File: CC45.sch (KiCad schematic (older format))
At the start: 20 parts

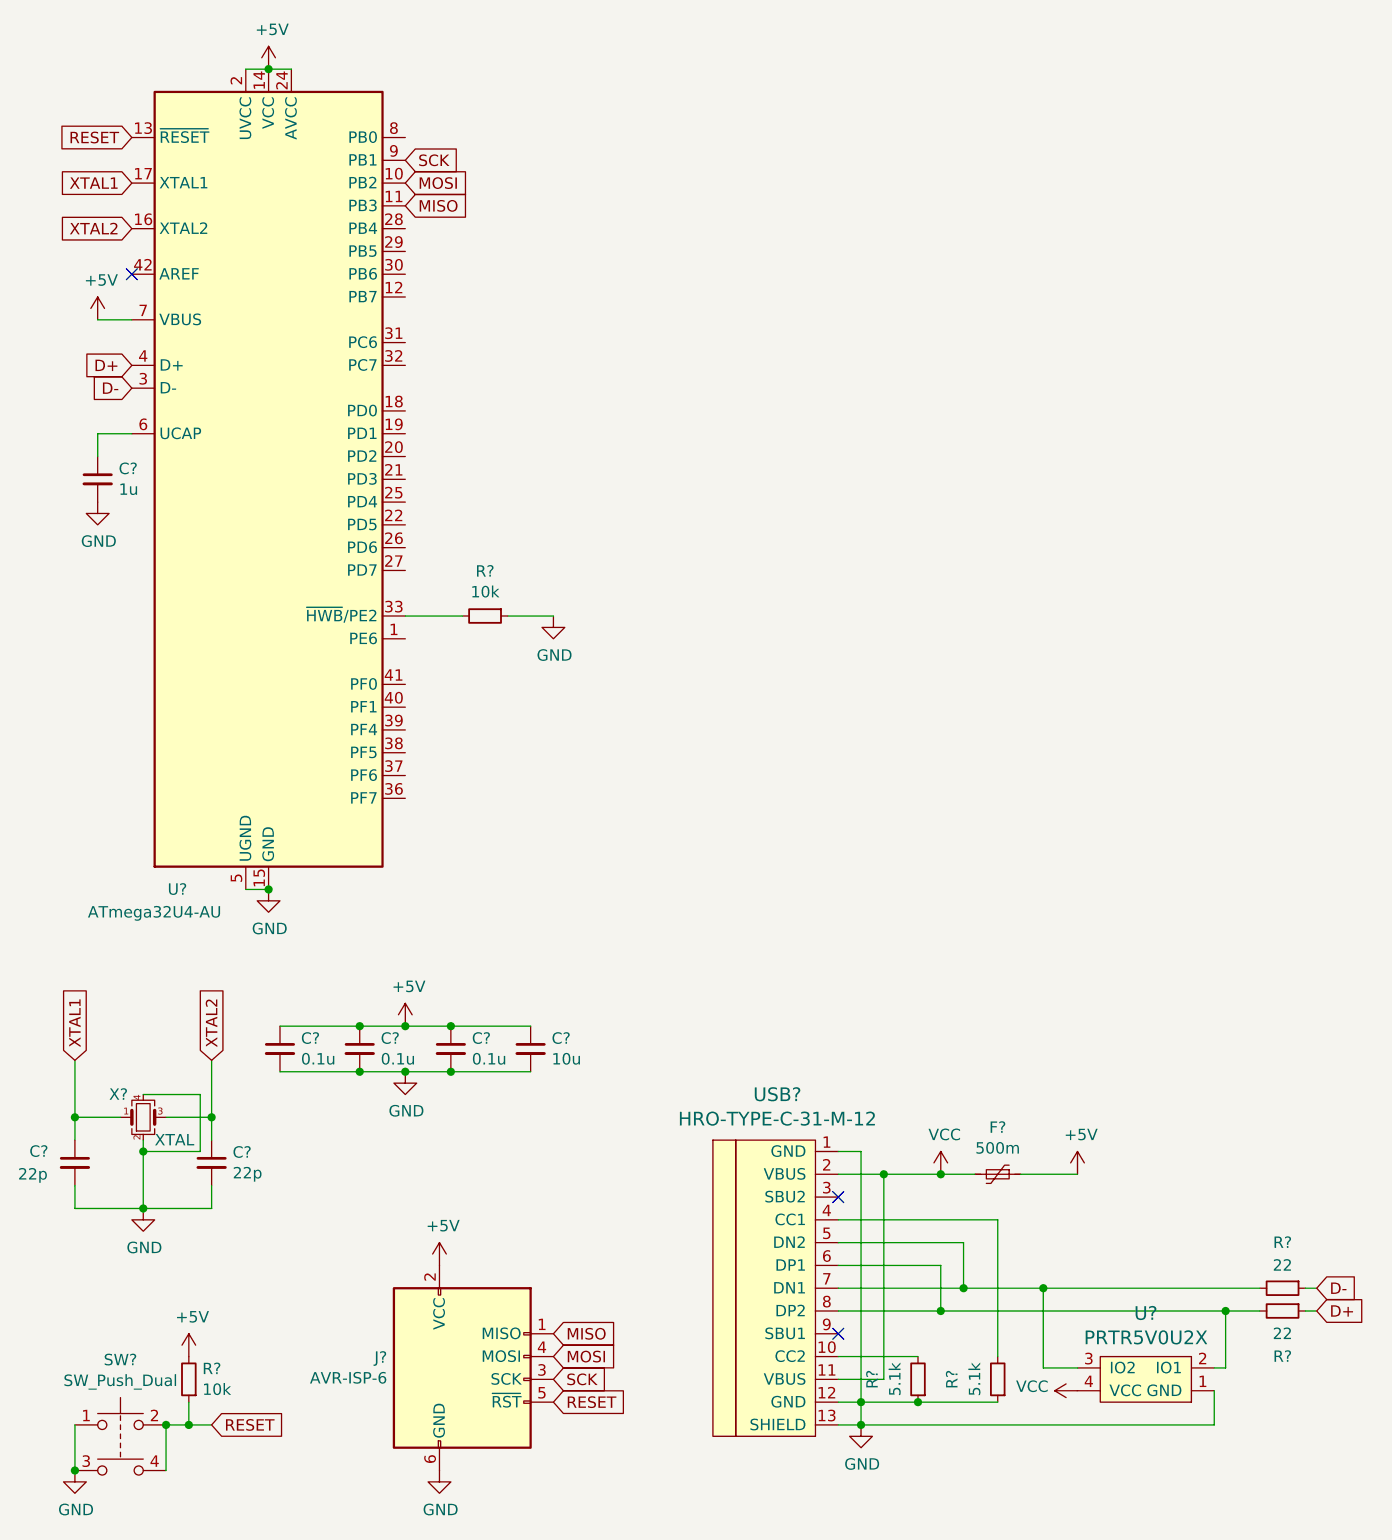
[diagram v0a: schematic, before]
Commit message: add switch matrix and assign footprints
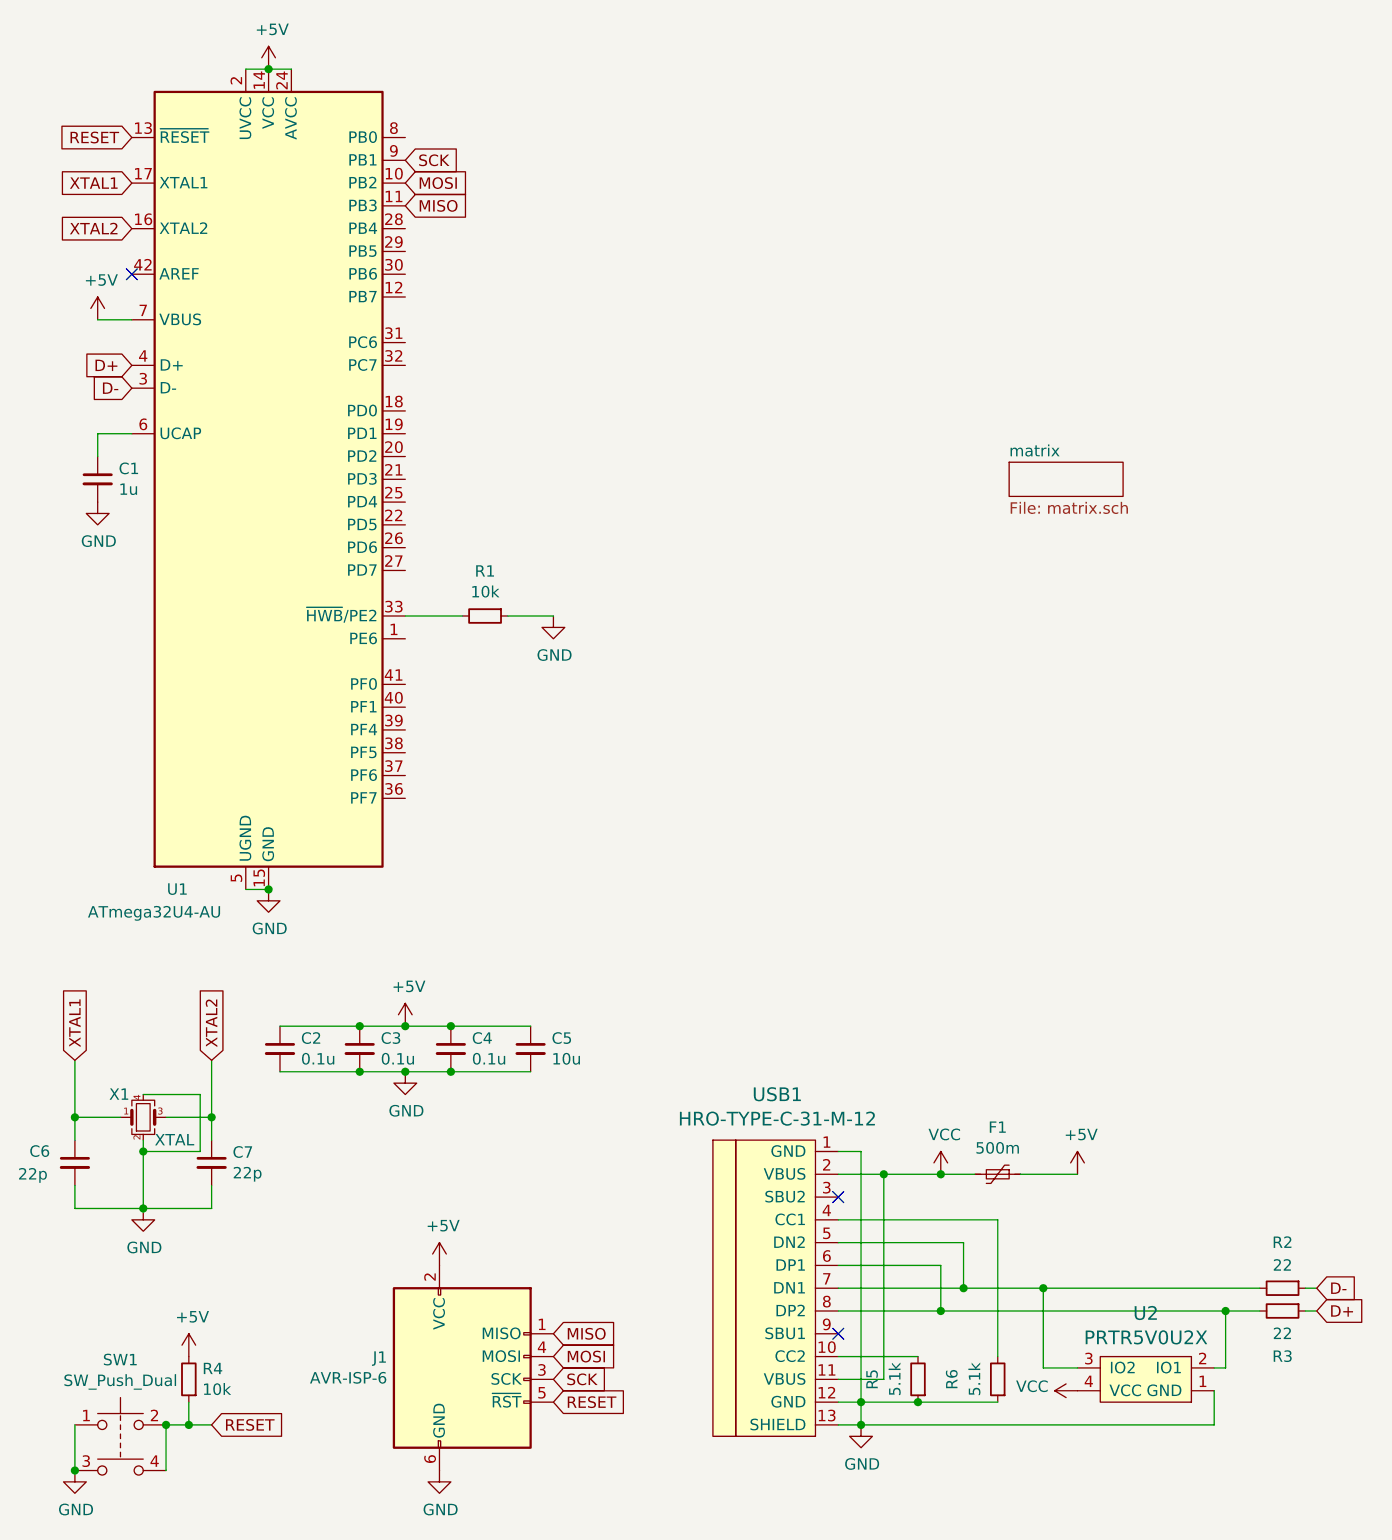
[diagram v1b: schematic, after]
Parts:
- removed C? (x2): 22p, symbol Device:C_Small
- removed C? (x2): 0.1u, symbol Device:C_Small
- removed R? (x2): 5.1k, symbol Device:R_Small
- removed R? (x2): 22, symbol Device:R_Small
- added C2, C3: 0.1u, Capacitor_SMD:C_1206_3216Metric_Pad1.42x1.75mm_HandSolder, symbol Device:C_Small
- added C6, C7: 22p, Capacitor_SMD:C_1206_3216Metric_Pad1.42x1.75mm_HandSolder, symbol Device:C_Small
- added R2, R3: 22, Resistor_SMD:R_1206_3216Metric_Pad1.42x1.75mm_HandSolder, symbol Device:R_Small
- added R5, R6: 5.1k, Resistor_SMD:R_1206_3216Metric_Pad1.42x1.75mm_HandSolder, symbol Device:R_Small
- C1, C4, C5: renamed from C?; footprint (none) -> Capacitor_SMD:C_1206_3216Metric_Pad1.42x1.75mm_HandSolder
- F1: renamed from F?; footprint (none) -> Fuse:Fuse_1206_3216Metric_Pad1.42x1.75mm_HandSolder
- J1: renamed from J?; footprint (none) -> random-keyboard-parts:Reset_Pretty-Mask
- R1, R4: renamed from R?; footprint (none) -> Resistor_SMD:R_1206_3216Metric_Pad1.42x1.75mm_HandSolder
- SW1: renamed from SW?; footprint (none) -> random-keyboard-parts:SKQG-1155865
- U2: renamed from U?; footprint (none) -> random-keyboard-parts:SKQGADE010
- USB1: renamed from USB?; footprint (none) -> Type-C:HRO-TYPE-C-31-M-12-HandSoldering
- X1: renamed from X?; footprint (none) -> Crystal:Crystal_SMD_3225-4Pin_3.2x2.5mm_HandSoldering
- gave numbers to parts that had none: 1
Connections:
- net +5V: now also C2.1, C3.1
- net D+: now also R3.1
- net D-: now also R2.1
- net GND: now also C2.2, C3.2, C6.2, C7.2, R5.1, R6.1
- net XTAL1: now also C6.1
- net XTAL2: now also C7.1
- net at USB1.10 (CC2): now also R5.2
- net at USB1.4 (CC1): now also R6.2
- net at U2.3 (IO2), USB1.5 (DN2), USB1.7 (DN1): now also R2.2
- net at U2.2 (IO1), USB1.6 (DP1), USB1.8 (DP2): now also R3.2
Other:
- moved on the sheet: C3, R2, R6

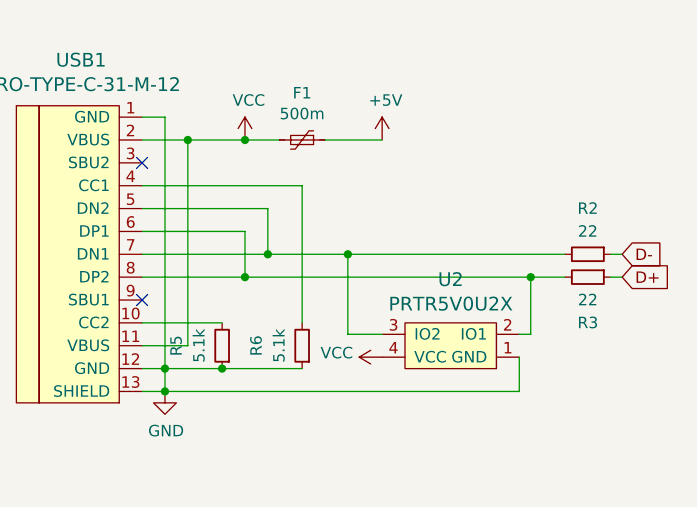
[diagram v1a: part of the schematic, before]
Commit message: Placed footprints on pcb and routed everything except the matrix
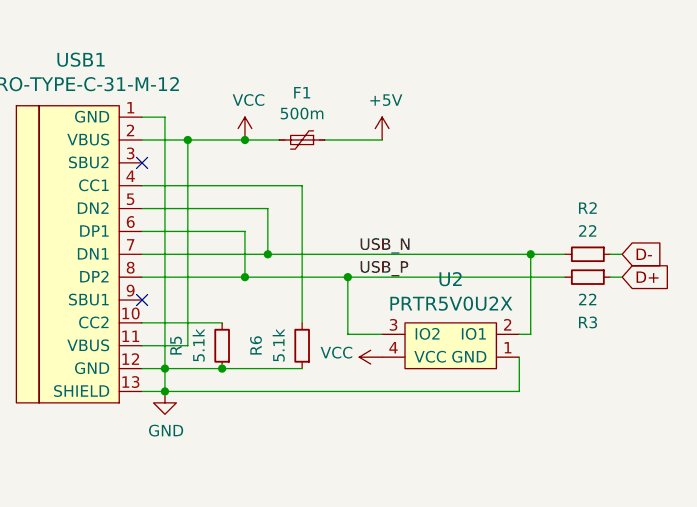
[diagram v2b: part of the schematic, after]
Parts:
- U2: footprint random-keyboard-parts:SKQGADE010 -> random-keyboard-parts:SOT143B
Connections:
- net USB_N: now reaches R2.2, USB1.5 (DN2), USB1.7 (DN1)
- net USB_N: now also U2.2 (IO1); no longer U2.3 (IO2)
- net USB_P: now reaches R3.2, USB1.6 (DP1), USB1.8 (DP2)
- net USB_P: now also U2.3 (IO2); no longer U2.2 (IO1)
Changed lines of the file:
@@
 Connection ~ 4900 6600
-Wire Wire Line
-	6300 6600 6150 6600
 Wire Wire Line
 	6500 6600 6550 6600
@@
 Text GLabel 6550 6600 2    50   Input ~ 0
 D+
-Wire Wire Line
-	6300 6500 5350 6500
 Wire Wire Line
 	6500 6500 6550 6500
@@
 $EndComp
 Connection ~ 4550 7100
-Connection ~ 5350 6500
-Wire Wire Line
-	5350 6500 5000 6500
-Connection ~ 6150 6600
-Wire Wire Line
-	6150 6600 4900 6600
 $Comp
 L power:VCC #PWR0116
@@
 F 0 "U2" H 5800 6611 60  0000 C CNN
 F 1 "PRTR5V0U2X" H 5800 6718 60  0000 C CNN
-F 2 "random-keyboard-parts:SKQGADE010" H 5800 6900 60  0001 C CNN
+F 2 "random-keyboard-parts:SOT143B" H 5800 6900 60  0001 C CNN
 F 3 "" H 5800 6900 60  0001 C CNN
 	1    5800 6900
@@
 	5500 6850 5350 6850
 Wire Wire Line
-	5350 6850 5350 6500
-Wire Wire Line
 	6100 7100 4550 7100
-Wire Wire Line
-	6150 6850 6150 6600
 Wire Wire Line
 	6100 6850 6150 6850
@@
 F1 "matrix.sch" 50
 $EndSheet
+Text Label 5400 6500 0    50   ~ 0
+USB_N
+Text Label 5400 6600 0    50   ~ 0
+USB_P
+Wire Wire Line
+	5350 6850 5350 6600
+Connection ~ 5350 6600
+Wire Wire Line
+	5350 6600 6300 6600
+Wire Wire Line
+	4900 6600 5350 6600
+Wire Wire Line
+	6150 6850 6150 6500
+Connection ~ 6150 6500
+Wire Wire Line
+	6150 6500 6300 6500
+Wire Wire Line
+	5000 6500 6150 6500
 $EndSCHEMATC

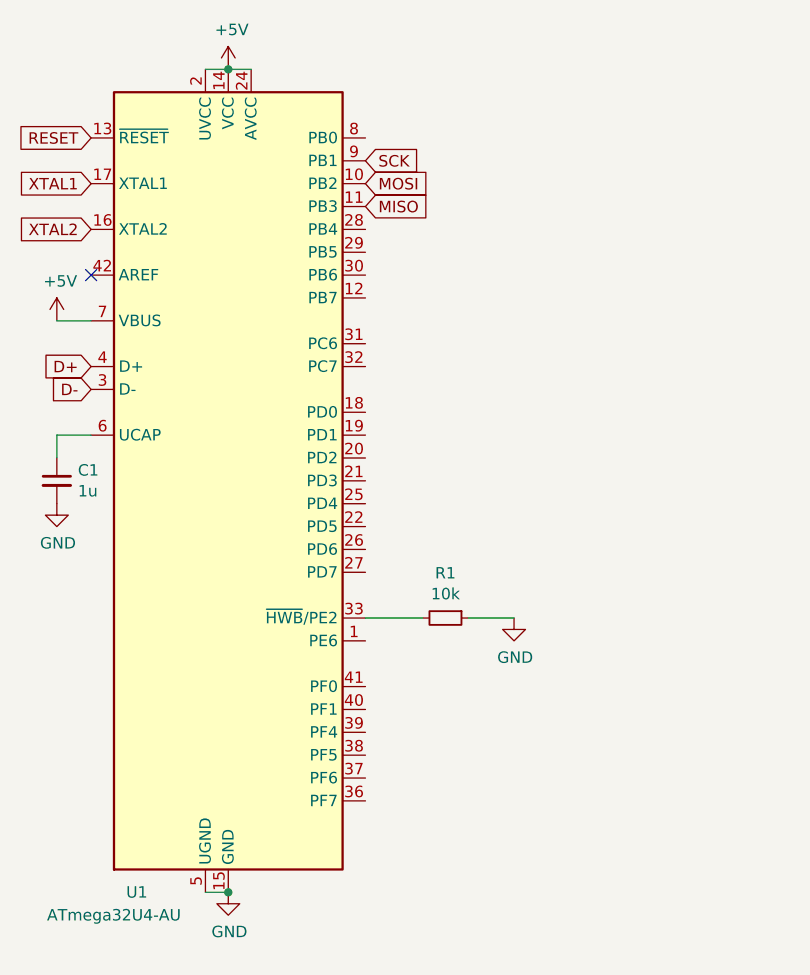
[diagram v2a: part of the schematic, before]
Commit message: Connect matrix to mcu on the schema and moved some components around
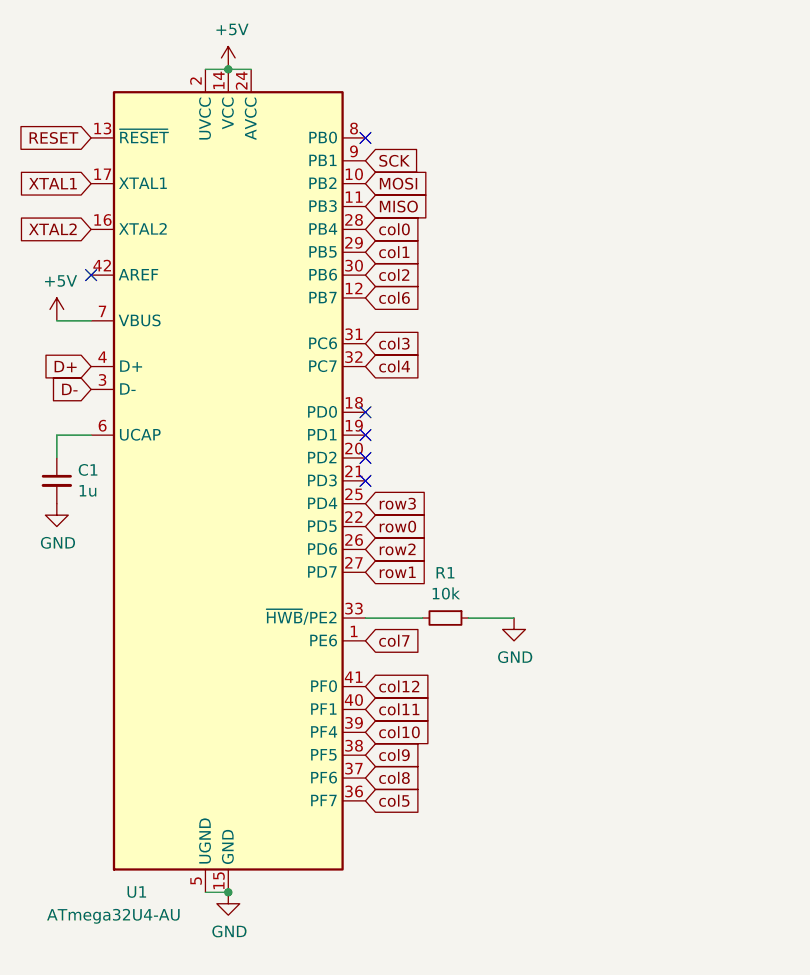
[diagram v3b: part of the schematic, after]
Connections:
- net col7: now reaches U1.1 (PE6)
- net col6: now reaches U1.12 (PB7)
- net row0: now reaches U1.22 (PD5)
- net row3: now reaches U1.25 (PD4)
- net row2: now reaches U1.26 (PD6)
- net row1: now reaches U1.27 (PD7)
- net col0: now reaches U1.28 (PB4)
- net col1: now reaches U1.29 (PB5)
- net col2: now reaches U1.30 (PB6)
- net col3: now reaches U1.31 (PC6)
- net col4: now reaches U1.32 (PC7)
- net col5: now reaches U1.36 (PF7)
- net col8: now reaches U1.37 (PF6)
- net col9: now reaches U1.38 (PF5)
- net col10: now reaches U1.39 (PF4)
- net col11: now reaches U1.40 (PF1)
- net col12: now reaches U1.41 (PF0)
- no-connect marks 3 -> 8
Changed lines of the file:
@@
 Wire Wire Line
 	5000 6500 6150 6500
+Text GLabel 2550 2150 2    50   Input ~ 0
+col6
+Text GLabel 2550 3250 2    50   Input ~ 0
+row2
+Text GLabel 2550 3850 2    50   Input ~ 0
+col12
+Text GLabel 2550 3950 2    50   Input ~ 0
+col11
+Text GLabel 2550 4050 2    50   Input ~ 0
+col10
+Text GLabel 2550 4150 2    50   Input ~ 0
+col9
+Text GLabel 2550 4250 2    50   Input ~ 0
+col8
+Text GLabel 2550 3650 2    50   Input ~ 0
+col7
+Text GLabel 2550 4350 2    50   Input ~ 0
+col5
+Text GLabel 2550 2450 2    50   Input ~ 0
+col4
+Text GLabel 2550 2350 2    50   Input ~ 0
+col3
+Text GLabel 2550 2050 2    50   Input ~ 0
+col2
+Text GLabel 2550 1950 2    50   Input ~ 0
+col1
+Text GLabel 2550 1850 2    50   Input ~ 0
+col0
+Text GLabel 2550 3150 2    50   Input ~ 0
+row0
+Text GLabel 2550 3350 2    50   Input ~ 0
+row1
+Text GLabel 2550 3050 2    50   Input ~ 0
+row3
+NoConn ~ 2550 2650
+NoConn ~ 2550 2750
+NoConn ~ 2550 2850
+NoConn ~ 2550 2950
+NoConn ~ 2550 1450
 $EndSCHEMATC

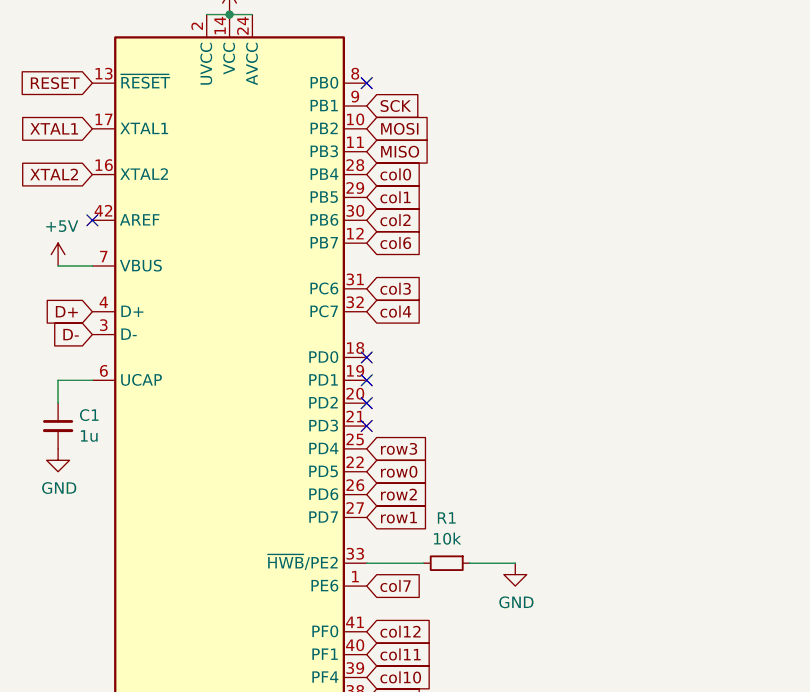
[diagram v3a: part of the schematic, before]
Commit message: Routed the matrix
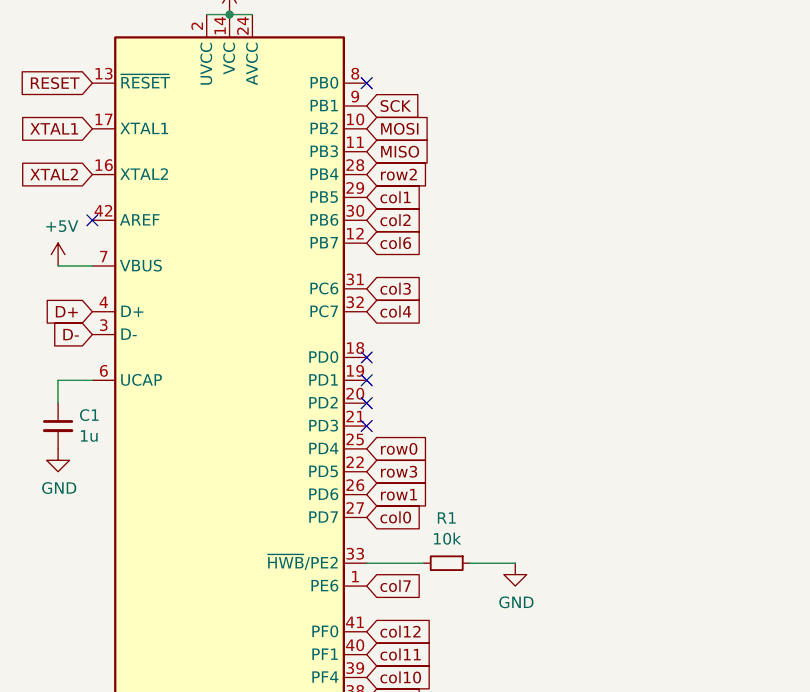
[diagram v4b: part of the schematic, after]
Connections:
- net col0: now also U1.27 (PD7); no longer U1.28 (PB4)
- net row0: now also U1.25 (PD4); no longer U1.22 (PD5)
- net row1: now also U1.26 (PD6); no longer U1.27 (PD7)
- net row2: now also U1.28 (PB4); no longer U1.26 (PD6)
- net row3: now also U1.22 (PD5); no longer U1.25 (PD4)
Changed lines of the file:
@@
 Text GLabel 2550 2150 2    50   Input ~ 0
 col6
-Text GLabel 2550 3250 2    50   Input ~ 0
+Text GLabel 2550 1850 2    50   Input ~ 0
 row2
 Text GLabel 2550 3850 2    50   Input ~ 0
@@
 Text GLabel 2550 1950 2    50   Input ~ 0
 col1
-Text GLabel 2550 1850 2    50   Input ~ 0
+Text GLabel 2550 3350 2    50   Input ~ 0
 col0
+Text GLabel 2550 3050 2    50   Input ~ 0
+row0
+Text GLabel 2550 3250 2    50   Input ~ 0
+row1
 Text GLabel 2550 3150 2    50   Input ~ 0
-row0
-Text GLabel 2550 3350 2    50   Input ~ 0
-row1
-Text GLabel 2550 3050 2    50   Input ~ 0
 row3
 NoConn ~ 2550 2650
